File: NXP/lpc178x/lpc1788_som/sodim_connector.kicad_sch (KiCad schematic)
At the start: 1 part, among them J1 SODIMM-200_Split

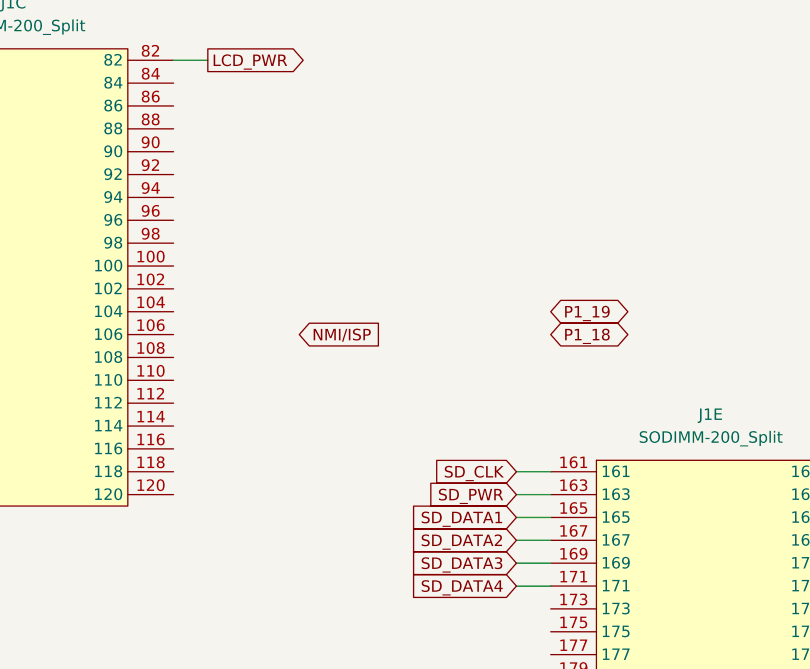
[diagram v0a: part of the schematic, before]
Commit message: LPC1788
Added LPC1788 som module
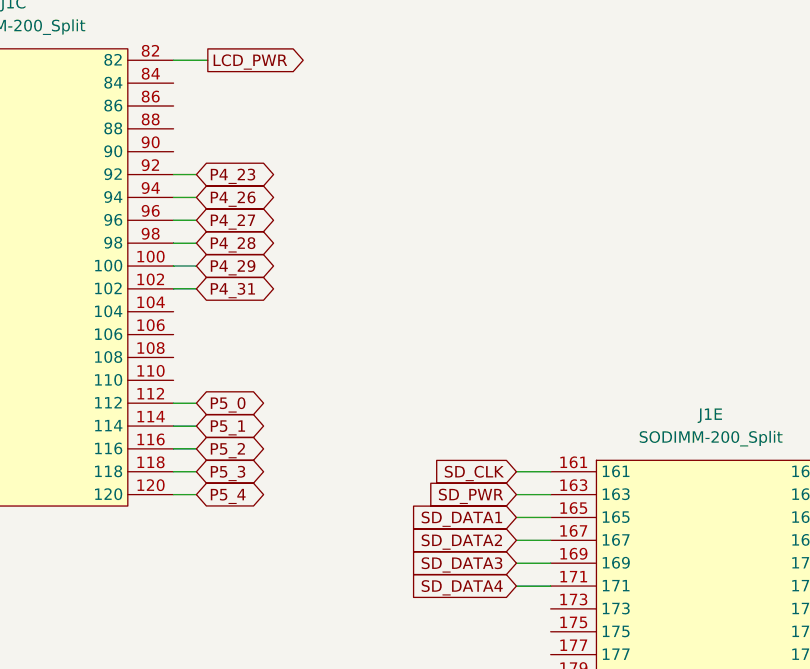
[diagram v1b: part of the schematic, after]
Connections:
- net P4_29: now reaches J1.100
- net P4_31: now reaches J1.102
- net P5_0: now reaches J1.112
- net P5_1: now reaches J1.114
- net P5_2: now reaches J1.116
- net P5_3: now reaches J1.118
- net P5_4: now reaches J1.120
- net P4_23: now reaches J1.92
- net P4_26: now reaches J1.94
- net P4_27: now reaches J1.96
- net P4_28: now reaches J1.98
